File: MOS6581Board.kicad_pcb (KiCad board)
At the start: 2 copper layers, 58.4 x 82.6 mm, 24 parts, among them J1 Board connector, J2 Power connector, U1 MOS6581, U2 LM7805_TO220, U3 MAX7375

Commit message: Add latest changes
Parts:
- removed REF** (x4): MountingHole_3.2mm_M3, Mounting_Holes:MountingHole_3.2mm_M3
- added C14: 10uF, Capacitors_SMD:C_0805_HandSoldering, F.Cu at (252.9, 47.4)
- added C15: 0.1uF, Capacitors_SMD:C_0805_HandSoldering, F.Cu at (252.9, 42.9)
- added C16: 0.1uF, Capacitors_SMD:C_0805_HandSoldering, F.Cu at (246.2, 66.4)
- added C17: 18pF, Capacitors_SMD:C_0805_HandSoldering, F.Cu at (-83.5, 33.2)
- added C18: 18pF, Capacitors_SMD:C_0805_HandSoldering, F.Cu at (-69.8, 51.2)
- added C19: .1uF, Capacitors_SMD:C_0805_HandSoldering, F.Cu at (162.2, 25.1)
- added C20: .1uF, Capacitors_SMD:C_0805_HandSoldering, F.Cu at (243.2, 65.7)
- added D1: LED, LEDs:LED_0805_HandSoldering, F.Cu at (195.8, 37.1)
- added D2: 1N4148, Diodes_SMD:D_SOD-323_HandSoldering, F.Cu at (-59.0, 29.3)
- added D3: POWER, LEDs:LED_0805_HandSoldering, F.Cu at (258.8, 35.0)
- added J10: CLOCK_TP, Pin_Headers:Pin_Header_Straight_1x01_Pitch1.27mm, F.Cu at (168.2, 89.1)
- added J3: DEBUG_UART, Pin_Headers:Pin_Header_Straight_1x03_Pitch2.54mm, F.Cu at (186.9, 33.9)
- added J4: MIDI_IN, Pin_Headers:Pin_Header_Straight_1x02_Pitch2.54mm, F.Cu at (-59.8, 34.0)
- added J5: JTAG, Pin_Headers:Pin_Header_Straight_2x05_Pitch2.54mm, F.Cu at (-30.8, 32.8)
- added J6: AUDIO_IN, Pin_Headers:Pin_Header_Straight_1x02_Pitch2.54mm, F.Cu at (1.75, 45.0)
- added J7: I2C, Pin_Headers:Pin_Header_Straight_1x02_Pitch2.54mm, F.Cu at (176.0, 30.9)
- added J8: GPIO, Pin_Headers:Pin_Header_Straight_1x04_Pitch1.27mm, F.Cu at (195.7, 44.6)
- added J9: RW_TP, Pin_Headers:Pin_Header_Straight_1x01_Pitch1.27mm, F.Cu at (172.7, 89.1)
- added L1: 10uH, Resistors_SMD:R_1206_HandSoldering, F.Cu at (252.9, 67.6)
- added R10: 4.7k, Resistors_SMD:R_0805_HandSoldering, F.Cu at (171.7, 23.2)
- added R11: 4.7k, Resistors_SMD:R_0805_HandSoldering, F.Cu at (176.0, 23.2)
- added R12: 2.2k, Resistors_SMD:R_0805_HandSoldering, F.Cu at (253.1, 35.0)
- added R3: 220, Resistors_SMD:R_0805_HandSoldering, F.Cu at (-62.3, 29.1)
- added R4: 2.2k, Resistors_SMD:R_0805_HandSoldering, F.Cu at (192.0, 37.1)
- added R5: 4.7k, Resistors_SMD:R_0805_HandSoldering, F.Cu at (-41.5, 26.6)
- added R6: 220, Resistors_SMD:R_0805_HandSoldering, F.Cu at (-41.5, 30.6)
- added R7: 1M, Resistors_SMD:R_0805_HandSoldering, F.Cu at (-73.5, 51.2)
- added R8: 27R, Resistors_SMD:R_0805_HandSoldering, F.Cu at (-83.5, 37.8)
- added R9: 10k, Resistors_SMD:R_0805_HandSoldering, F.Cu at (178.2, 89.1)
- added SW1: SW_Push, Buttons_Switches_THT:SW_PUSH_6mm, F.Cu at (160.2, 36.9)
- added U4: ATMEGA2560-16AU, Housings_QFP:TQFP-100_14x14mm_Pitch0.5mm, F.Cu at (67.5, 84.8)
- added Y1: 16MHz, Crystals:Crystal_SMD_HC49-SD_HandSoldering, F.Cu at (-75.5, 44.2)
- C1, C8: value 1uF -> 10uF; footprint Capacitors_SMD:C_0805_HandSoldering -> Capacitors_THT:CP_Radial_D5.0mm_P2.50mm
- C2, C3: value 470pf -> 470pF; footprint Capacitors_SMD:C_0805_HandSoldering -> Resistors_THT:R_Axial_DIN0614_L14.3mm_D5.7mm_P20.32mm_Horizontal
- J1: value Board connector -> AUDIO_OUT; footprint Pin_Headers:Pin_Header_Straight_2x10_Pitch2.54mm -> Pin_Headers:Pin_Header_Straight_1x02_Pitch2.54mm
- U3: value MAX7375 -> 6N138SM; footprint TO_SOT_Packages_SMD:SOT-323_SC-70_Handsoldering -> Housings_DIP:SMDIP-8_W7.62mm
- moved R2 232.5 mm to (256.4, 75.8)
- moved C13 227.5 mm to (252.9, 51.9), turned to 0 degrees
- moved C7 218.1 mm to (252.9, 60.1), turned to 0 degrees
- moved C11 197.2 mm to (252.9, 63.9), turned to 0 degrees
- moved C12 197.0 mm to (252.9, 56.1), turned to 0 degrees
- moved C2 118.9 mm to (-85.8, 67.0)
- moved J2 105.8 mm to (143.3, 53.3), turned to 90 degrees
- moved C6 105.7 mm to (143.2, 68.0)
- moved C3 97.5 mm to (-65.5, 76.2), turned to 180 degrees
- moved C9 92.5 mm to (143.2, 74.8), turned to 0 degrees
- moved C10 92.4 mm to (143.2, 71.8), turned to 0 degrees
- moved C5 92.3 mm to (143.3, 90.3), turned to 90 degrees
- moved C4 90.1 mm to (139.8, 90.3), turned to 90 degrees
- moved C8 89.7 mm to (-25.8, 70.8), turned to 270 degrees
- moved C1 88.2 mm to (-20.8, 56.5)
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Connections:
- C1 pad 2: /AUDIOOUT -> /AUDIO_OUT
- C2 pad 1: /CAP1A -> /CAP1B
- C2 pad 2: /CAP1B -> /CAP1A
- C3 pad 1: /CAP2A -> /CAP2B
- C3 pad 2: /CAP2B -> /CAP2A
- C8 pad 1: /_EXTIN -> /AUDIO_IN
- J1 pad 1: /~RW -> /AUDIO_OUT
- J1 pad 2: /A0 -> GND
- U1 pad 26: /_EXTIN -> /EXTIN
- U3 pad 1: +5V -> Net-(U3-Pad1)
- U3 pad 2: /CLOCK -> Net-(D2-Pad1)
- U3 pad 3: GND -> /MIDI_IN_C
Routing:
- net GND: track 113.5 -> 0.00 mm, vias 4 -> 0
- net +5V: track 84.7 -> 0.00 mm
- net /AUDIOOUT: track 53.8 -> 0.00 mm
- net /~RES: track 48.0 -> 0.00 mm, vias 1 -> 0
- net +12V: track 38.2 -> 0.00 mm
- net /D7: track 35.7 -> 0.00 mm
- net /EXTIN: track 33.2 -> 0.00 mm
- net /~RW: track 32.4 -> 0.00 mm
- net /D6: track 31.3 -> 0.00 mm
- net /A0: track 29.2 -> 0.00 mm
- net /~CS: track 27.7 -> 0.00 mm
- net /A1: track 27.3 -> 0.00 mm
- net /D5: track 27.0 -> 0.00 mm
- net Net-(C1-Pad1): track 22.6 -> 0.00 mm
- net /_EXTIN: track 21.9 -> 0.00 mm
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- removed copper zone on B.Cu, net GND
- removed copper zone on F.Cu, net GND
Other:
- board size 58.4 x 82.6 mm -> 100 x 100 mm
- board text added: "MOS6581 board v02 Croft D'Andrea DiPietro 2018"
- board text removed: "MOS6581 board v01 Croft D'Andrea DiPietro 2018"

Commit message: laid out general paths for data and address lines.
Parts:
- moved U3 201.1 mm to (132.1, 112.9)
- moved J5 125.5 mm to (82.9, 86.1), turned to 90 degrees
- moved C2 115.0 mm to (21.7, 26.1)
- moved C3 96.3 mm to (21.7, 35.3), turned to 0 degrees
- moved SW1 35.8 mm to (124.5, 36.2)
- moved J6 33.1 mm to (-31.3, 45.8)
- moved U4 7.11 mm to (64.5, 91.2)
- moved U1 5.84 mm to (55.0, 41.4)
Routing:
- net /D7: track 0.00 -> 126.3 mm
- net /~CS: track 0.00 -> 125.2 mm, vias 0 -> 1
- net /D6: track 0.00 -> 117.6 mm
- net /D5: track 0.00 -> 110.1 mm
- net /D4: track 0.00 -> 102.5 mm
- net /D3: track 0.00 -> 90.7 mm
- net /D2: track 0.00 -> 80.4 mm
- net /D1: track 0.00 -> 75.1 mm
- net /D0: track 0.00 -> 70.1 mm
- net /A0: track 0.00 -> 69.6 mm, vias 0 -> 1
- net /A1: track 0.00 -> 67.0 mm, vias 0 -> 1
- net /A2: track 0.00 -> 63.5 mm, vias 0 -> 1
- net /A3: track 0.00 -> 59.6 mm, vias 0 -> 1
- net /A4: track 0.00 -> 56.0 mm, vias 0 -> 1
- net /CLOCK: track 0.00 -> 36.4 mm
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
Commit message: Add auto-routed PCB
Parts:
- moved C17 172.6 mm to (77.8, 94.8)
- moved R8 172.6 mm to (77.8, 99.2)
- moved J8 167.9 mm to (34.7, 92.3)
- moved C18 167.1 mm to (92.8, 90.2)
- moved R7 167.1 mm to (89.0, 90.2)
- moved D2 157.4 mm to (92.2, 72.8)
- moved R3 157.4 mm to (89.0, 72.5)
- moved J4 157.3 mm to (90.8, 79.8), turned to 0 degrees
- moved C11 154.0 mm to (100.4, 85.1)
- moved C12 154.0 mm to (100.4, 77.4)
- moved C13 154.0 mm to (100.4, 73.1)
- moved C14 154.0 mm to (100.4, 68.6)
- moved C15 154.0 mm to (100.4, 64.1)
- moved C7 154.0 mm to (100.4, 81.4)
- moved L1 154.0 mm to (100.4, 88.9)
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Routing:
- net GND: track 0.00 -> 416.6 mm, vias 0 -> 2
- net +5V: track 0.00 -> 206.3 mm
- net /~RES: track 0.00 -> 128.5 mm, vias 0 -> 1
- net /SCL: track 0.00 -> 102.9 mm, vias 0 -> 1
- net /MIDI_UART_RX: track 0.00 -> 98.1 mm, vias 0 -> 2
- net /SDA: track 0.00 -> 95.8 mm, vias 0 -> 1
- net Net-(C1-Pad1): track 0.00 -> 93.1 mm, vias 0 -> 1
- net Net-(C18-Pad1): track 0.00 -> 87.5 mm
- net /D7: track 126.3 -> 44.3 mm, vias 0 -> 1
- net /~CS: track 125.2 -> 46.4 mm
- net /D6: track 117.6 -> 41.5 mm, vias 0 -> 1
- net Net-(C17-Pad1): track 0.00 -> 73.2 mm
- net /D4: track 102.5 -> 36.4 mm, vias 0 -> 1
- net /D5: track 110.1 -> 44.3 mm, vias 0 -> 1
- net Net-(C20-Pad1): track 0.00 -> 64.0 mm, vias 0 -> 2
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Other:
- board size 100 x 100 mm -> 111.8 x 100.2 mm

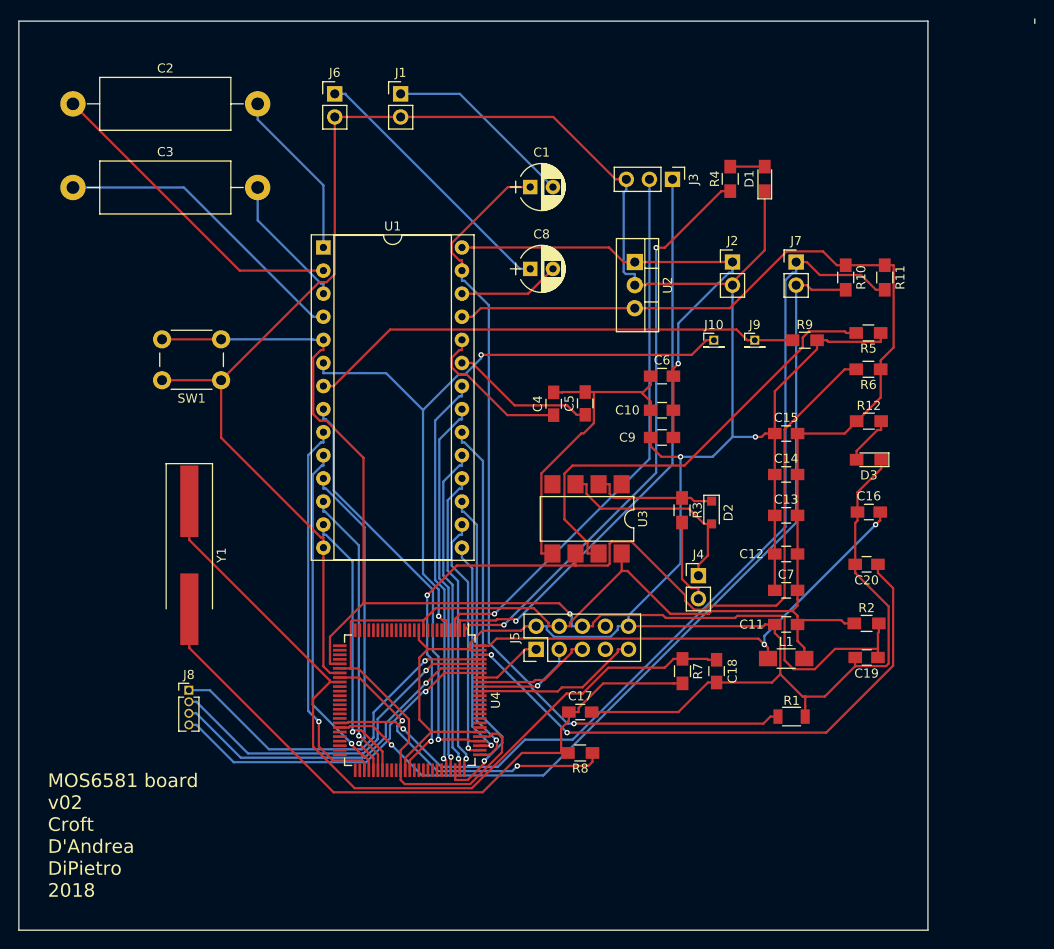
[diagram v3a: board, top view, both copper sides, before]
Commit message: Attempt a tighter board layout
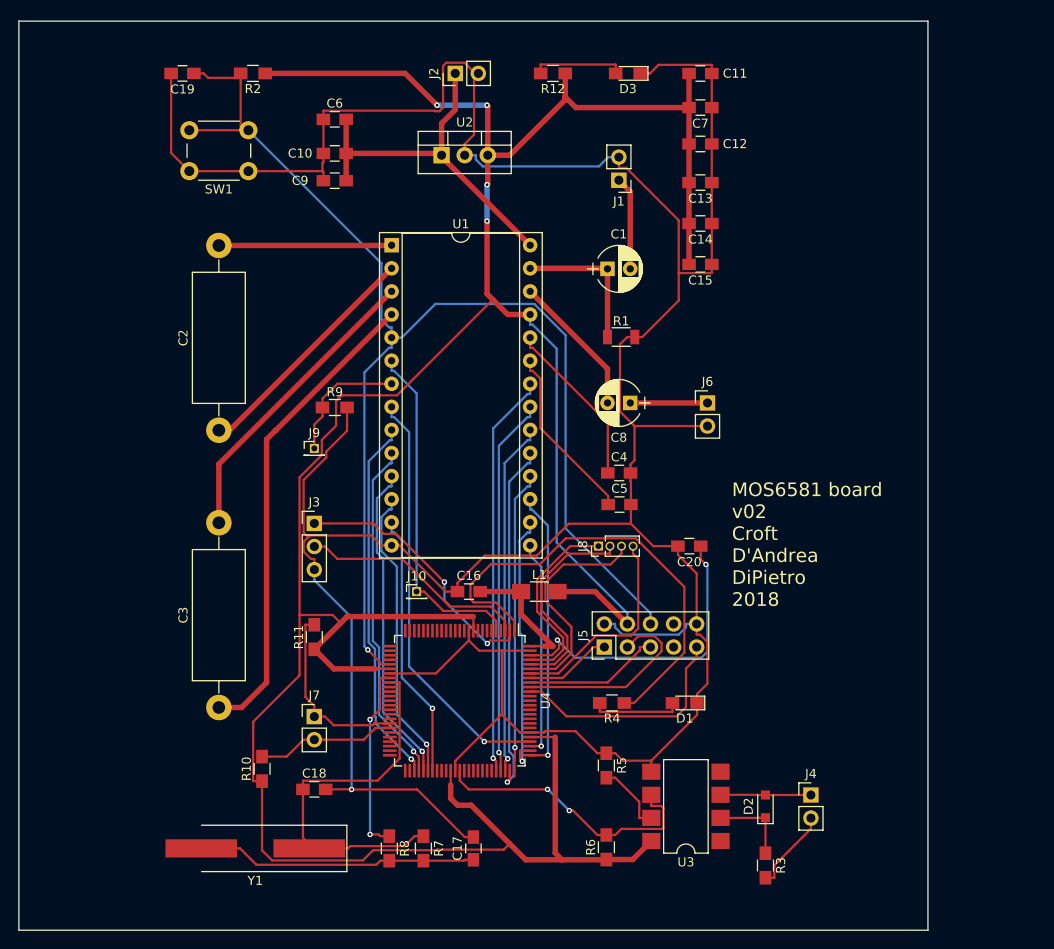
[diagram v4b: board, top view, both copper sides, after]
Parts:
- moved C19 98.9 mm to (34.0, 24.5)
- moved R2 90.6 mm to (41.8, 24.5), turned to 180 degrees
- moved R10 83.9 mm to (42.8, 101.0), turned to 90 degrees
- moved R11 74.2 mm to (48.5, 86.5), turned to 90 degrees
- moved J7 72.9 mm to (48.5, 95.2)
- moved C11 61.3 mm to (91.0, 24.5), turned to 180 degrees
- moved R6 60.0 mm to (80.6, 109.6), turned to 90 degrees
- moved C3 59.4 mm to (38.0, 94.2), turned to 90 degrees
- moved R4 59.1 mm to (81.2, 93.8), turned to 180 degrees
- moved D1 58.3 mm to (89.2, 93.8), turned to 180 degrees
- moved R5 55.6 mm to (80.6, 100.6), turned to 270 degrees
- moved J3 54.6 mm to (48.5, 74.0), turned to 0 degrees
- moved C7 53.9 mm to (91.0, 28.3), turned to 180 degrees
- moved J6 53.3 mm to (91.8, 60.8)
- moved R9 52.2 mm to (50.8, 61.2)
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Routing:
- net +5V: track 206.3 -> 334.2 mm, vias 0 -> 4
- net /SCL: track 102.9 -> 20.3 mm, vias 1 -> 0
- net /SDA: track 95.8 -> 15.4 mm, vias 1 -> 0
- net Net-(C1-Pad1): track 93.1 -> 16.0 mm, vias 1 -> 0
- net /MIDI_UART_RX: track 98.1 -> 31.1 mm
- net Net-(C18-Pad1): track 87.5 -> 42.1 mm
- net Net-(R5-Pad2): track 50.3 -> 7.81 mm
- net Net-(C17-Pad1): track 73.2 -> 30.9 mm
- net /~RW: track 54.7 -> 14.1 mm
- net +5VA: track 53.5 -> 14.5 mm, vias 2 -> 0
- net /CLOCK: track 74.6 -> 37.9 mm, vias 2 -> 0
- net GND: track 416.6 -> 381.3 mm, vias 2 -> 1
- net /DEBUG_UART_TX: track 60.7 -> 25.5 mm, vias 1 -> 0
- net /DEBUG_UART_RX: track 63.1 -> 29.4 mm, vias 1 -> 2
- net Net-(C20-Pad1): track 64.0 -> 34.0 mm
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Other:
- board size 111.8 x 100.2 mm -> 100 x 100 mm

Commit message: cleaned up layout.
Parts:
- moved C13 65.9 mm to (52.5, 90.0), turned to 0 degrees
- moved C15 64.1 mm to (64.8, 104.0)
- moved C14 59.5 mm to (77.5, 99.0), turned to 90 degrees
- moved C12 56.3 mm to (64.7, 82.1), turned to 0 degrees
- moved J3 36.6 mm to (84.7, 79.6), turned to 180 degrees
- moved C11 29.2 mm to (78.8, 51.0)
- moved C6 24.8 mm to (73.5, 39.5), turned to 180 degrees
- moved J6 24.6 mm to (90.4, 36.2), turned to 180 degrees
- moved D1 21.9 mm to (78.8, 74.5)
- moved J5 20.5 mm to (100.0, 93.5), turned to 270 degrees
- moved C8 18.5 mm to (90.3, 43.6), turned to 270 degrees
- moved C7 18.1 mm to (73.6, 33.5)
- moved C5 16.1 mm to (78.8, 56.2)
- moved R4 15.2 mm to (77.5, 79.0), turned to 90 degrees
- moved C4 15.2 mm to (78.8, 53.6)
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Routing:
- net /~RES: track 144.5 -> 225.5 mm
- net +5V: track 334.2 -> 391.2 mm
- net /DEBUG_LED: track 52.5 -> 10.8 mm, vias 0 -> 2
- net /TCK: track 9.61 -> 32.1 mm
- net Net-(C20-Pad1): track 34.0 -> 12.2 mm, vias 2 -> 0
- net /PF2: track 24.8 -> 10.3 mm
- net /POTY: track 19.5 -> 5.35 mm
- net /POTX: track 18.6 -> 5.33 mm
- net /PF1: track 23.3 -> 10.6 mm
- net /PF3: track 23.3 -> 10.6 mm
- net /MIDI_UART_RX: track 31.1 -> 42.5 mm
- net /DEBUG_UART_RX: track 29.4 -> 18.1 mm
- net /TMS: track 15.1 -> 26.1 mm, vias 0 -> 1
- net /PF0: track 21.3 -> 10.9 mm
- net /TDI: track 25.8 -> 18.1 mm
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- added copper zone on B.Cu, net GND
- added copper zone on F.Cu, net GND
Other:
- board text added: "+"
- board text added: "-"
- board text added: "Audio In"
- board text added: "Audio Out"
- board text added: "Clock"
- board text added: "Debug UART"
- board text added: "GPIO"
- board text added: "JTAG"
- board text added: "MIDI IN"
- board text added: "Power"
- board text added: "RX"
- board text added: "Reset"
- board text added: "SCL"
- board text added: "SDA"
- board text added: "TX"
- board text added: "~RW"

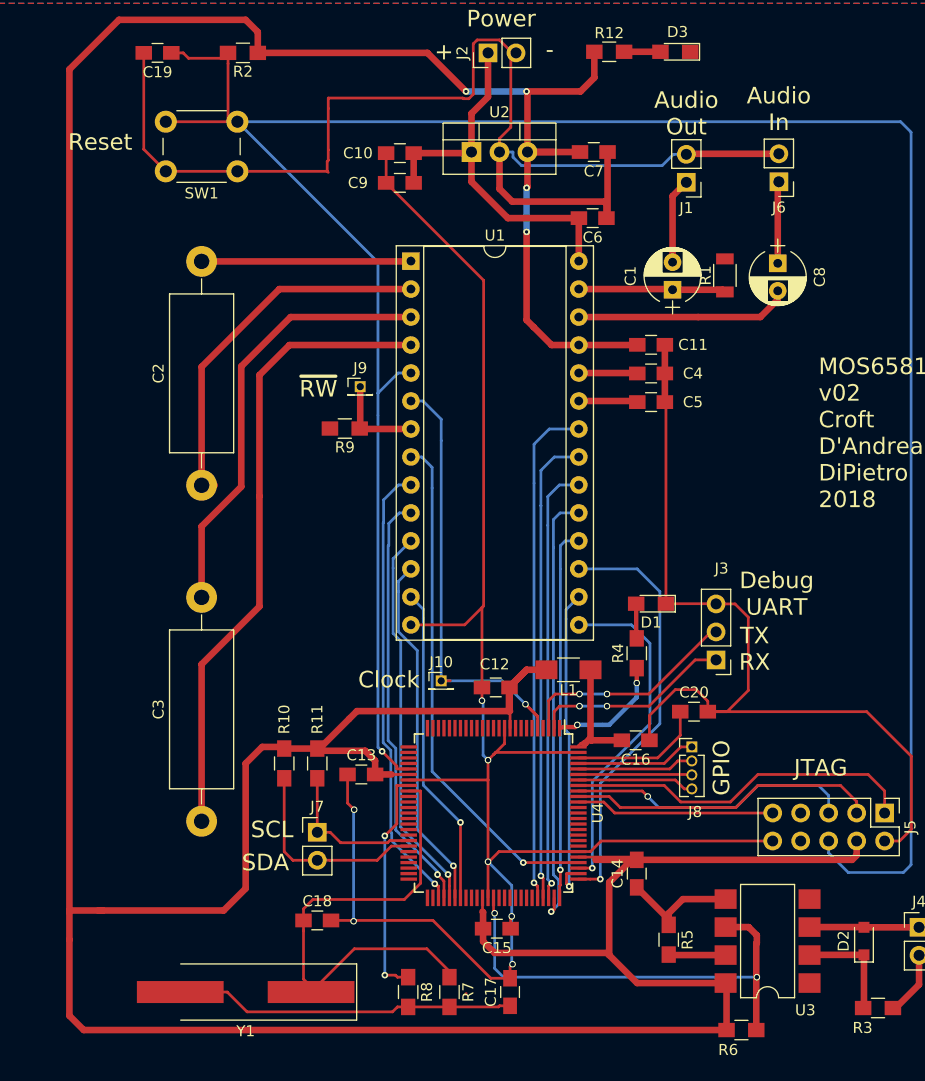
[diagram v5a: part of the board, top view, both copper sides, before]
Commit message: did a little more cleanup around the crystal oscillator.
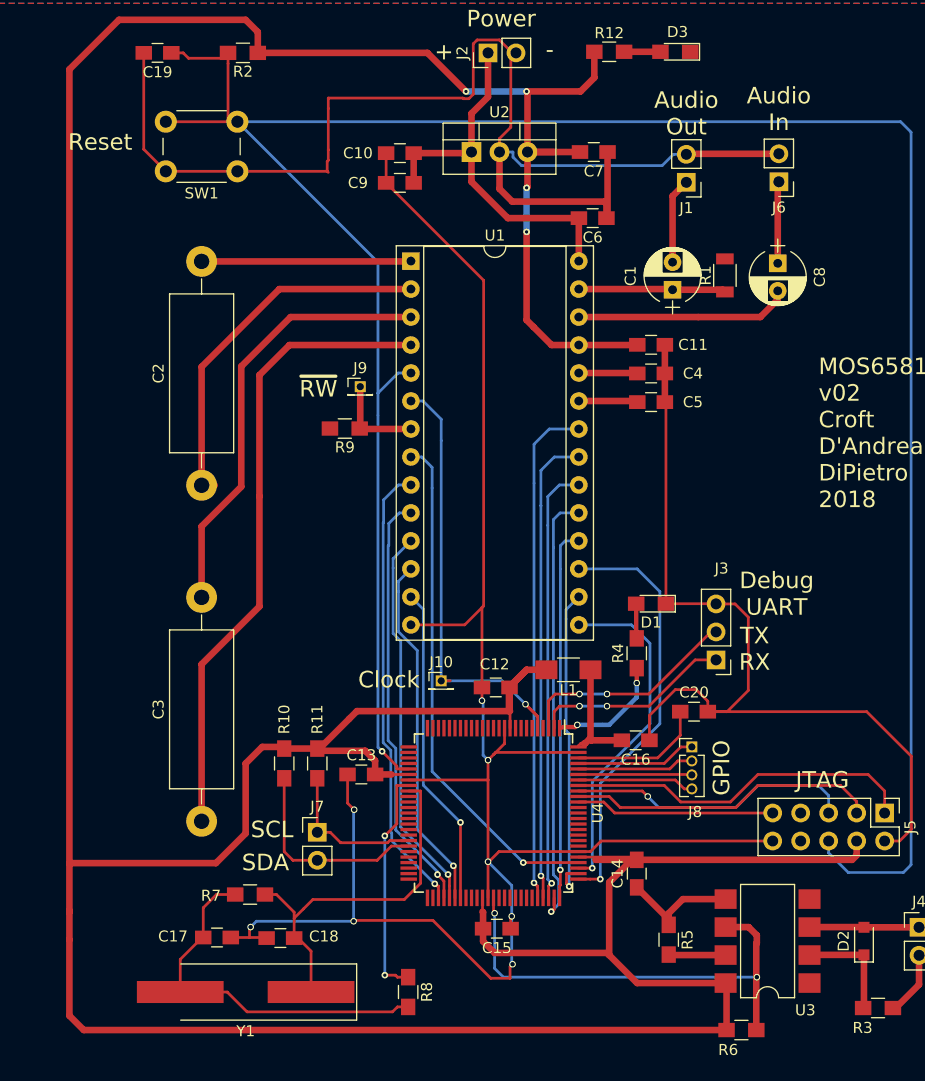
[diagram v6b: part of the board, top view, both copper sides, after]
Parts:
- moved C17 27.1 mm to (39.4, 104.8), turned to 0 degrees
- moved R7 20.1 mm to (42.4, 100.9), turned to 180 degrees
- moved C18 3.71 mm to (45.1, 104.8), turned to 180 degrees
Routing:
- net GND: track 375.3 -> 387.0 mm, vias 7 -> 8
- net Net-(C18-Pad1): track 45.1 -> 34.1 mm
- net +5V: track 391.2 -> 386.2 mm
- net Net-(C17-Pad1): track 30.9 -> 33.6 mm
